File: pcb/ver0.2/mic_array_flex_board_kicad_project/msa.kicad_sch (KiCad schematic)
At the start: 25 parts, among them U2 MP23DB01HPTR, U5 MP23DB01HPTR, U6 MP23DB01HPTR, U7 MP23DB01HPTR

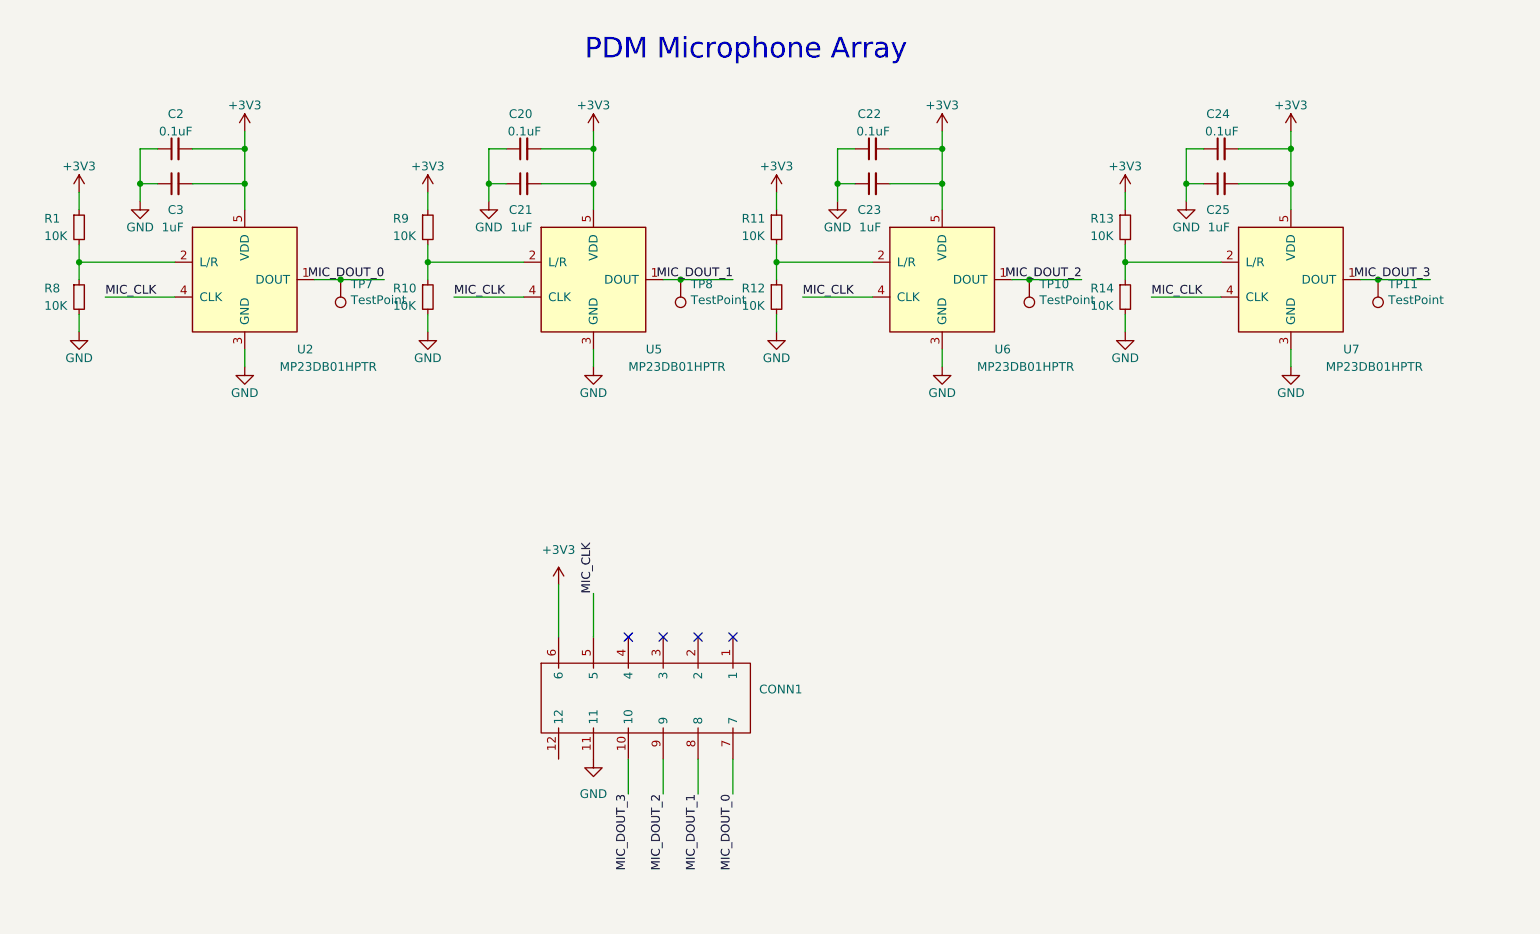
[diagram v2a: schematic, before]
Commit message: last changes setup for manufacturing for v0p2 - only step left is spacing of microphones
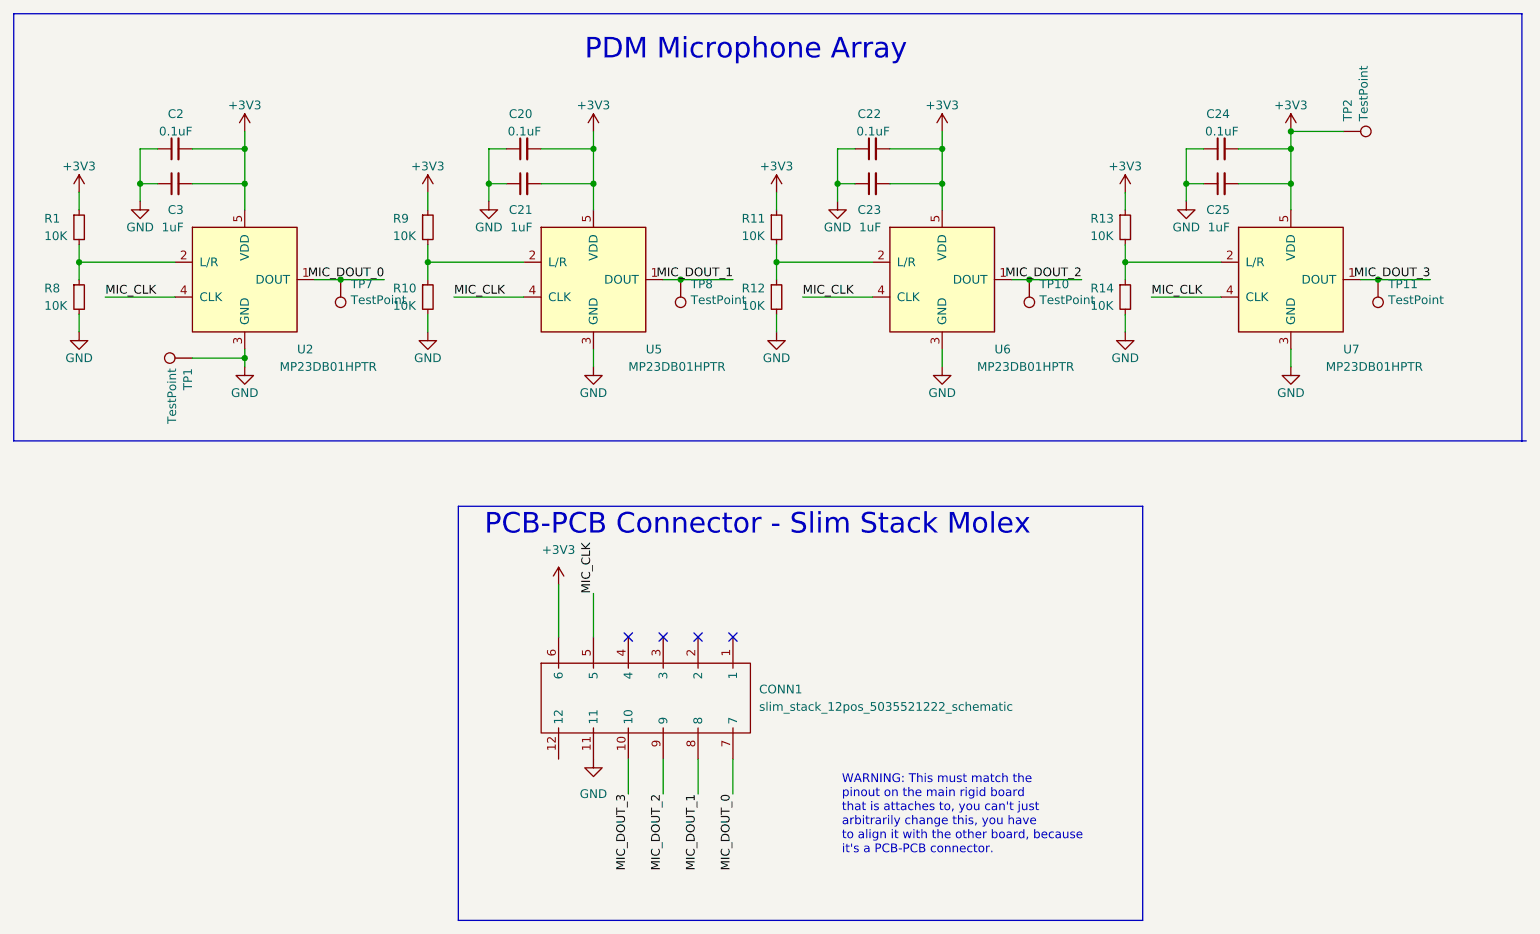
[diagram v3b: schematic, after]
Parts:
- added TP1, TP2: TestPoint, mico:SMD_1x01_P1.27mm, symbol Connector:TestPoint
- CONN1: value (none) -> slim_stack_12pos_5035521222_schematic; footprint (none) -> OpenSourceSmartGlasses:slim_stack_molex_PLUG_5035521222
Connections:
- net +3V3: now also TP2.1
- net GND: now also TP1.1
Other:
- note added: "PCB-PCB Connector - Slim Stack Molex"
- note added: "WARNING: This must match the pinout on the main rigid board that is attaches to, you can't just arbitrarily change this, you have to align it with the other board, because it's a PCB-PCB connector."
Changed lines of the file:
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@@
   (junction (at 203.2 34.29) (diameter 0) (color 0 0 0 0)
   )
+  (junction (at 50.8 64.77) (diameter 0) (color 0 0 0 0)
+  )
   (junction (at 128.27 50.8) (diameter 0) (color 0 0 0 0)
   )
@@
   )
   (junction (at 101.6 39.37) (diameter 0) (color 0 0 0 0)
+  )
+  (junction (at 203.2 31.75) (diameter 0) (color 0 0 0 0)
   )
   (junction (at 77.47 50.8) (diameter 0) (color 0 0 0 0)
@@
     (stroke (width 0) (type default) (color 0 0 0 0))
   )
+  (wire (pts (xy 203.2 31.75) (xy 210.82 31.75))
+    (stroke (width 0) (type default) (color 0 0 0 0))
+  )
   (wire (pts (xy 86.36 34.29) (xy 88.9 34.29))
     (stroke (width 0) (type default) (color 0 0 0 0))
@@
     (stroke (width 0) (type default) (color 0 0 0 0))
   )
+  (polyline (pts (xy 81.915 86.36) (xy 181.61 86.36))
+    (stroke (width 0) (type default) (color 0 0 0 0))
+  )
   (wire (pts (xy 86.36 39.37) (xy 86.36 41.91))
     (stroke (width 0) (type default) (color 0 0 0 0))
@@
     (stroke (width 0) (type default) (color 0 0 0 0))
   )
+  (polyline (pts (xy 236.855 76.835) (xy 17.145 76.835))
+    (stroke (width 0) (type default) (color 0 0 0 0))
+  )
   (wire (pts (xy 195.58 39.37) (xy 203.2 39.37))
     (stroke (width 0) (type default) (color 0 0 0 0))
@@
     (stroke (width 0) (type default) (color 0 0 0 0))
   )
+  (polyline (pts (xy 236.855 76.835) (xy 237.49 76.835))
+    (stroke (width 0) (type default) (color 0 0 0 0))
+  )
   (wire (pts (xy 64.77 53.34) (xy 71.12 53.34))
     (stroke (width 0) (type default) (color 0 0 0 0))
   )
+  (wire (pts (xy 50.8 64.77) (xy 43.18 64.77))
+    (stroke (width 0) (type default) (color 0 0 0 0))
+  )
   (wire (pts (xy 128.27 43.18) (xy 128.27 40.64))
     (stroke (width 0) (type default) (color 0 0 0 0))
@@
     (stroke (width 0) (type default) (color 0 0 0 0))
   )
+  (polyline (pts (xy 181.61 86.36) (xy 181.61 146.685))
+    (stroke (width 0) (type default) (color 0 0 0 0))
+  )
   (wire (pts (xy 35.56 39.37) (xy 35.56 34.29))
     (stroke (width 0) (type default) (color 0 0 0 0))
@@
     (stroke (width 0) (type default) (color 0 0 0 0))
   )
+  (polyline (pts (xy 181.61 146.685) (xy 81.915 146.685))
+    (stroke (width 0) (type default) (color 0 0 0 0))
+  )
   (wire (pts (xy 77.47 53.34) (xy 77.47 50.8))
     (stroke (width 0) (type default) (color 0 0 0 0))
   )
+  (polyline (pts (xy 236.855 14.605) (xy 236.855 76.835))
+    (stroke (width 0) (type default) (color 0 0 0 0))
+  )
+  (polyline (pts (xy 17.145 14.605) (xy 236.855 14.605))
+    (stroke (width 0) (type default) (color 0 0 0 0))
+  )
   (wire (pts (xy 91.44 55.88) (xy 81.28 55.88))
     (stroke (width 0) (type default) (color 0 0 0 0))
@@
     (stroke (width 0) (type default) (color 0 0 0 0))
   )
-  (wire (pts (xy 50.8 63.5) (xy 50.8 66.04))
+  (wire (pts (xy 50.8 63.5) (xy 50.8 64.77))
+    (stroke (width 0) (type default) (color 0 0 0 0))
+  )
+  (wire (pts (xy 50.8 64.77) (xy 50.8 66.04))
+    (stroke (width 0) (type default) (color 0 0 0 0))
+  )
+  (polyline (pts (xy 81.915 86.36) (xy 81.915 146.685))
     (stroke (width 0) (type default) (color 0 0 0 0))
   )
@@
     (stroke (width 0) (type default) (color 0 0 0 0))
   )
+  (polyline (pts (xy 17.145 76.835) (xy 17.145 14.605))
+    (stroke (width 0) (type default) (color 0 0 0 0))
+  )
   (wire (pts (xy 86.36 39.37) (xy 86.36 34.29))
     (stroke (width 0) (type default) (color 0 0 0 0))
@@
   (wire (pts (xy 128.27 58.42) (xy 128.27 60.96))
     (stroke (width 0) (type default) (color 0 0 0 0))
+  )
+  (text "WARNING: This must match the\npinout on the main rigid board\nthat is attaches to, you can't just\narbitrarily change this, you have\nto align it with the other board, because\nit's a PCB-PCB connector.\n"
+    (at 137.795 137.16 0)
+    (effects (font (size 1.27 1.27)) (justify left bottom))
+  )
+  (text "PCB-PCB Connector - Slim Stack Molex\n" (at 85.725 90.805 0)
+    (effects (font (size 3 3)) (justify left bottom))
   )
   (text "PDM Microphone Array" (at 100.33 21.59 0)
@@
       (effects (font (size 1.27 1.27)) (justify left))
     )
-    (property "Value" "" (id 1) (at 125.73 115.5699 0)
-      (effects (font (size 1.27 1.27)) (justify left))
-    )
-    (property "Footprint" "" (id 2) (at 104.14 96.52 0)
+    (property "Value" "slim_stack_12pos_5035521222_schematic" (id 1) (at 125.73 115.5699 0)
+      (effects (font (size 1.27 1.27)) (justify left))
+    )
+    (property "Footprint" "OpenSourceSmartGlasses:slim_stack_molex_PLUG_5035521222" (id 2) (at 104.14 96.52 0)
       (effects (font (size 1.27 1.27)) hide)
     )
@@
     (pin "1")
   )
+  (symbol (lib_id "Connector:TestPoint") (at 43.18 64.77 90) (unit 1)
+    (in_bom yes) (on_board yes)
+    (property "Reference" "TP1" (id 0) (at 42.5196 66.2432 0)
+      (effects (font (size 1.27 1.27)) (justify right))
+    )
+    (property "Value" "TestPoint" (id 1) (at 40.2082 66.2432 0)
+      (effects (font (size 1.27 1.27)) (justify right))
+    )
+    (property "Footprint" "mico:SMD_1x01_P1.27mm" (id 2) (at 43.18 59.69 0)
+      (effects (font (size 1.27 1.27)) hide)
+    )
+    (property "Datasheet" "~" (id 3) (at 43.18 59.69 0)
+      (effects (font (size 1.27 1.27)) hide)
+    )
+    (pin "1")
+  )
   (symbol (lib_name "GND_1") (lib_id "power:GND") (at 101.6 123.19 0) (unit 1)
     (in_bom yes) (on_board yes) (fields_autoplaced)
@@
     (pin "1")
   )
+  (symbol (lib_id "Connector:TestPoint") (at 210.82 31.75 270) (unit 1)
+    (in_bom yes) (on_board yes)
+    (property "Reference" "TP2" (id 0) (at 211.4804 30.2768 0)
+      (effects (font (size 1.27 1.27)) (justify right))
+    )
+    (property "Value" "TestPoint" (id 1) (at 213.7918 30.2768 0)
+      (effects (font (size 1.27 1.27)) (justify right))
+    )
+    (property "Footprint" "mico:SMD_1x01_P1.27mm" (id 2) (at 210.82 36.83 0)
+      (effects (font (size 1.27 1.27)) hide)
+    )
+    (property "Datasheet" "~" (id 3) (at 210.82 36.83 0)
+      (effects (font (size 1.27 1.27)) hide)
+    )
+    (pin "1")
+  )
   (sheet_instances
     (path "/" (page "1"))
@@
       (reference "R14") (unit 1) (value "10K") (footprint "Resistor_SMD:R_0402_1005Metric")
     )
+    (path "/d48a1f87-90e2-4ea0-aae2-d1ddc0abc032"
+      (reference "TP1") (unit 1) (value "TestPoint") (footprint "mico:SMD_1x01_P1.27mm")
+    )
+    (path "/e50bea87-2ea4-4103-bf2c-e4feffb9f20a"
+      (reference "TP2") (unit 1) (value "TestPoint") (footprint "mico:SMD_1x01_P1.27mm")
+    )
     (path "/00000000-0000-0000-0000-00006206d2d0"
